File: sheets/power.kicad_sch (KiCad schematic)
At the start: 81 parts, among them J4 POWER JACK, Q11 C1815, Q12 A1015, Q13 A1442, SW2 POWER SWITCH, T1 SH-302, U11 74LS05, U12 74LS06, U28 PC4741, U29 PC4741, U33 74AS04, U37 LM2576T-5, U38 74HC32, U8 74HC04, U80 74HC04

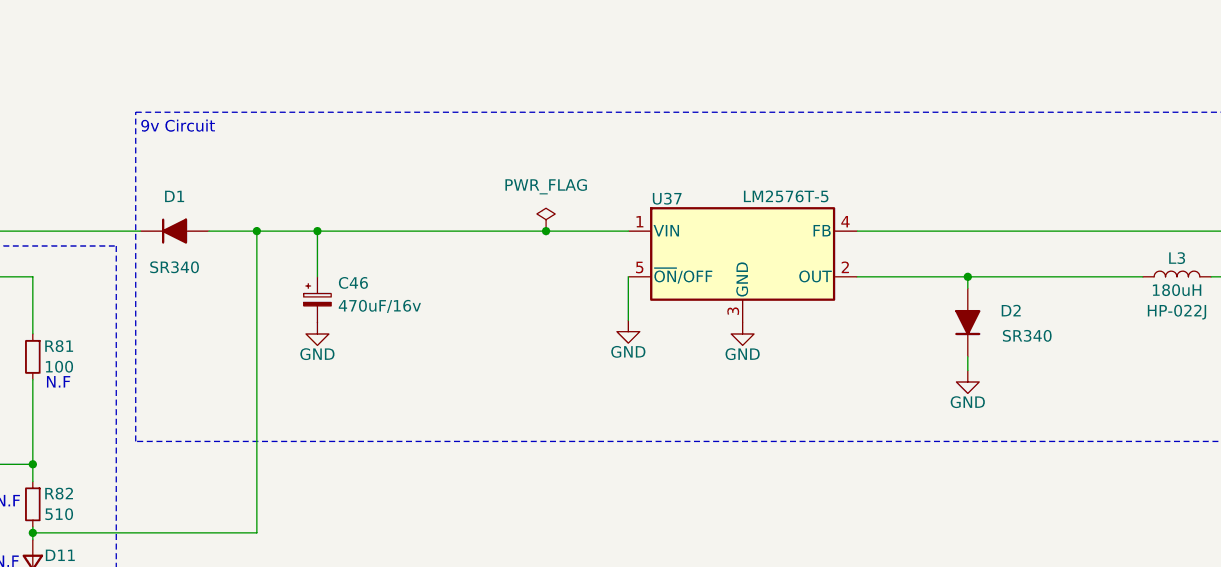
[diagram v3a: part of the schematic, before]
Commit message: Schematic fixes to PCB for D1 and D2
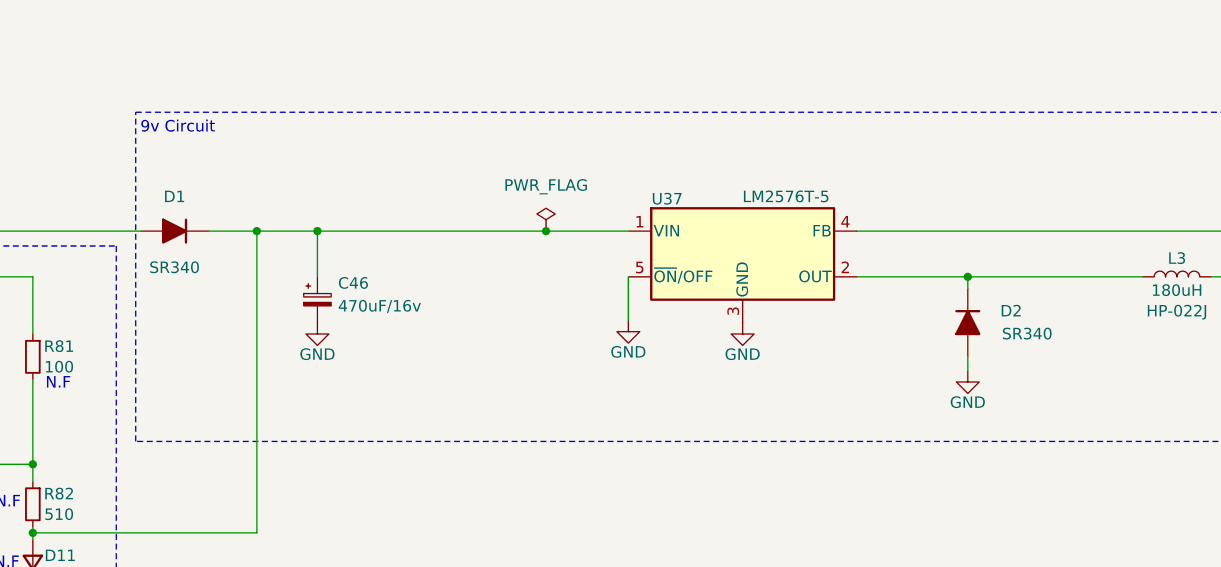
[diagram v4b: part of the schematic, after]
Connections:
- net GND: now also D2.2 (A); no longer D2.1 (K)
- net at C46.1, D11.2 (A), R82.2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: now also D1.1 (K); no longer D1.2 (A)
- net at L3.1, U37.2 (OUT): now also D2.1 (K); no longer D2.2 (A)
- net at D13.2 (A), Q12.1 (E), R77.2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: now also D1.2 (A); no longer D1.1 (K)
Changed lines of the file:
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@@
     )
   )
-  (symbol (lib_id "Device:D_Filled") (at 212.852 70.866 90) (unit 1)
+  (symbol (lib_id "Device:D_Filled") (at 212.852 70.866 90) (mirror x) (unit 1)
     (in_bom yes) (on_board yes) (dnp no)
     (property "Reference" "D2" (at 217.678 69.596 90)
       (effects (font (size 1.27 1.27)))
     )
-    (property "Value" "SR340" (at 219.456 72.39 90)
+    (property "Value" "SR340" (at 219.456 72.136 90)
       (effects (font (size 1.27 1.27)))
     )
@@
     )
   )
-  (symbol (lib_id "Device:D_Filled") (at 124.714 60.706 0) (unit 1)
+  (symbol (lib_id "Device:D_Filled") (at 124.714 60.706 0) (mirror y) (unit 1)
     (in_bom yes) (on_board yes) (dnp no)
     (property "Reference" "D1" (at 124.714 56.896 0)

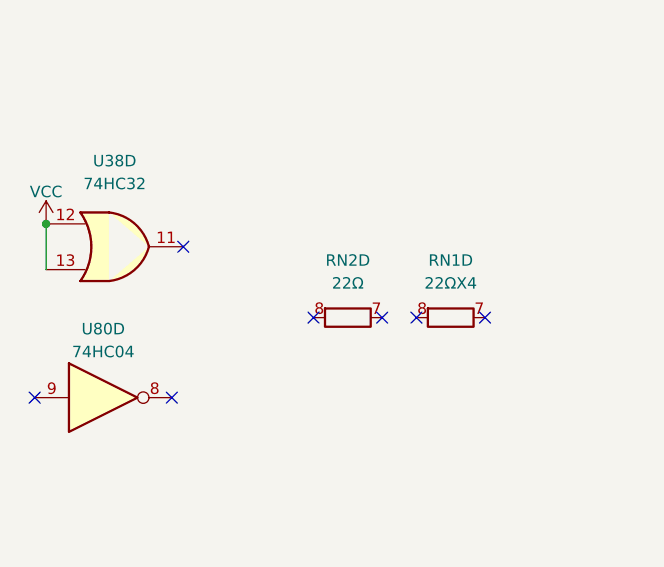
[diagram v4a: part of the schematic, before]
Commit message: More silkscreen tidy up, adding mouser components to BOM
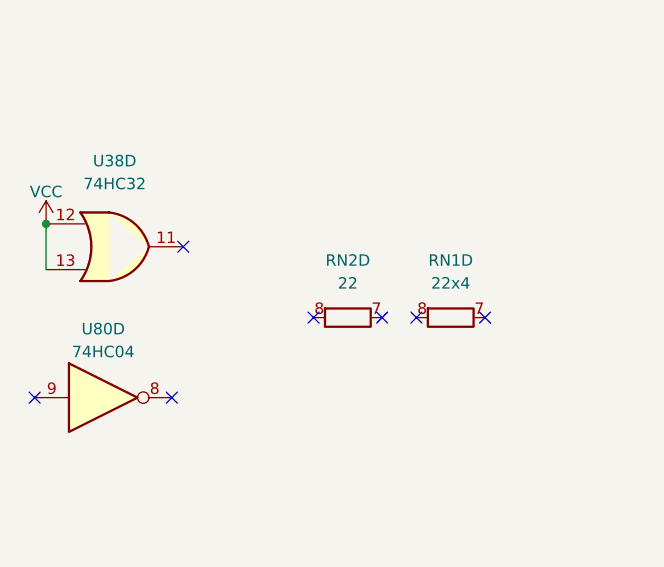
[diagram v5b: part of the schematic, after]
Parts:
- C46: Mouser (none) -> 647-UHE1C471MPD6
- D1, D2: Mouser (none) -> 583-SR340-T
- RN1: value 22ΩX4 -> 22x4
- RN2: value 22Ω -> 22
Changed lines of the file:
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@@
       (effects (font (size 1.27 1.27)))
     )
-    (property "Value" "22Ω" (at 370.078 226.06 90)
+    (property "Value" "22" (at 370.078 226.06 90)
       (effects (font (size 1.27 1.27)))
     )
@@
       (effects (font (size 1.27 1.27)) hide)
     )
-    (property "Mouser" "" (at 140.589 68.326 0)
+    (property "Mouser" "647-UHE1C471MPD6" (at 140.589 68.326 0)
       (effects (font (size 1.27 1.27)) hide)
     )
@@
       (effects (font (size 1.27 1.27)) hide)
     )
-    (property "Mouser" "" (at 212.852 70.866 0)
+    (property "Mouser" "583-SR340-T" (at 212.852 70.866 0)
       (effects (font (size 1.27 1.27)) hide)
     )
@@
       (effects (font (size 1.27 1.27)) hide)
     )
-    (property "Mouser" "" (at 124.714 60.706 0)
+    (property "Mouser" "583-SR340-T" (at 124.714 60.706 0)
       (effects (font (size 1.27 1.27)) hide)
     )
@@
       (effects (font (size 1.27 1.27)))
     )
-    (property "Value" "22ΩX4" (at 381.508 226.06 90)
-      (effects (font (size 1.27 1.27)))
-    )
+    (property "Value" "22x4" (at 381.508 226.06 90)
+      (effects (font (size 1.27 1.27)))
+    )

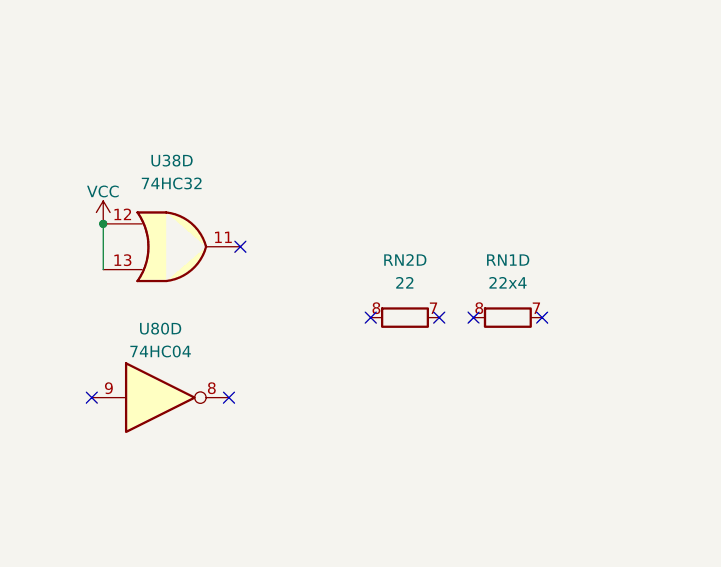
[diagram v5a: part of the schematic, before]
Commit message: Little tweaks to silkscreen Updated BOM with mouser parts
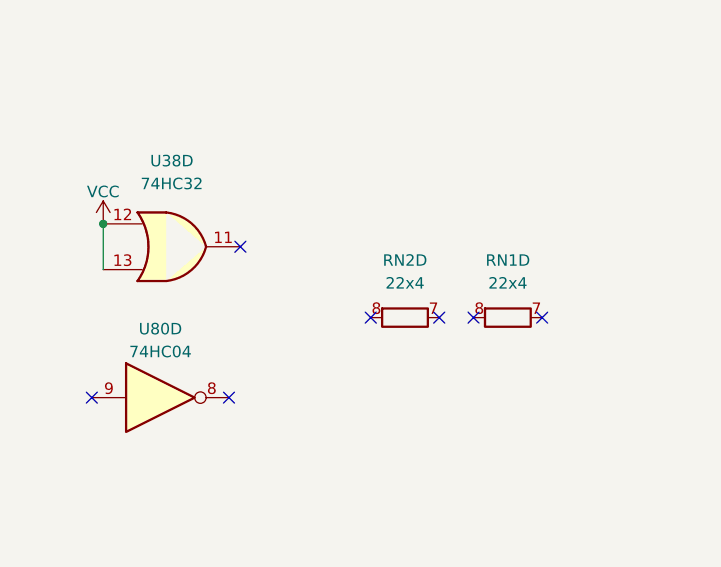
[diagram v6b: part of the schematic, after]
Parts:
- D5: Mouser (none) -> 604-WP7113ID5V
- H1, H10, H11, H12, H13, H14, H16, H17, H18, H2, H3, H4, H5, H6, H7, H8, H9: now left out of the parts list
- J4: Mouser (none) -> 490-PJ-102B
- RN1: Mouser (none) -> 652-4608X-2LF-22
- RN2: value 22 -> 22x4; Mouser (none) -> 652-4608X-2LF-22
- SW2, U28, U29: Comment (none) -> Use Original
- T1: Mouser (none) -> 80-SH-302
- U11: Mouser (none) -> 595-SN74LS05N
- U12: Mouser (none) -> 595-SN74LS06N
- U33: Mouser (none) -> 595-SN74AS04N
- U37: Alternative (none) -> https://www.aliexpress.com/item/1005004285746293.html
- U38: Mouser (none) -> 595-SN74HC32N
- U8, U80: Mouser (none) -> 595-SN74HC04N

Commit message: update before public
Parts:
- U37: Mouser (none) -> 926-LM2576T-5.0/NOPB
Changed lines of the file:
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@@
       (effects (font (size 1.27 1.27)) hide)
     )
-    (property "Mouser" "" (at 187.833 63.246 0)
+    (property "Mouser" "926-LM2576T-5.0/NOPB" (at 187.833 63.246 0)
       (effects (font (size 1.27 1.27)) hide)
     )

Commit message: Tweaks to BOM
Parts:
- R76: Comment Not Fitted when 9v Circuit -> (none); Mouser (none) -> 71-CMF501K0000FHEA
- R78: Comment Not Fitted when 9v Circuit -> R78 Not Fitted when 9v Circuit; Mouser (none) -> 71-CMF501K0000FHEA
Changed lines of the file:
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@@
       (effects (font (size 1.27 1.27)) hide)
     )
-    (property "Comment" "Not Fitted when 9v Circuit" (at 51.562 80.137 0)
-      (effects (font (size 1.27 1.27)) hide)
-    )
-    (property "Mouser" "" (at 51.562 80.137 0)
+    (property "Comment" "R78 Not Fitted when 9v Circuit" (at 51.562 80.137 0)
+      (effects (font (size 1.27 1.27)) hide)
+    )
+    (property "Mouser" "71-CMF501K0000FHEA" (at 51.562 80.137 0)
       (effects (font (size 1.27 1.27)) hide)
     )
@@
       (effects (font (size 1.27 1.27)) hide)
     )
-    (property "Comment" "Not Fitted when 9v Circuit" (at 180.34 111.125 0)
-      (effects (font (size 1.27 1.27)) hide)
-    )
-    (property "Mouser" "" (at 180.34 111.125 0)
-      (effects (font (size 1.27 1.27)) hide)
-    )
+    (property "Comment" "" (at 180.34 111.125 0)
+      (effects (font (size 1.27 1.27)) hide)
+    )
+    (property "Mouser" "71-CMF501K0000FHEA" (at 180.34 111.125 0)
+      (effects (font (size 1.27 1.27)) hide)
+    )
